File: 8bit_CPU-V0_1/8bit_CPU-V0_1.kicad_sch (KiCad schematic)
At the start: 0 parts

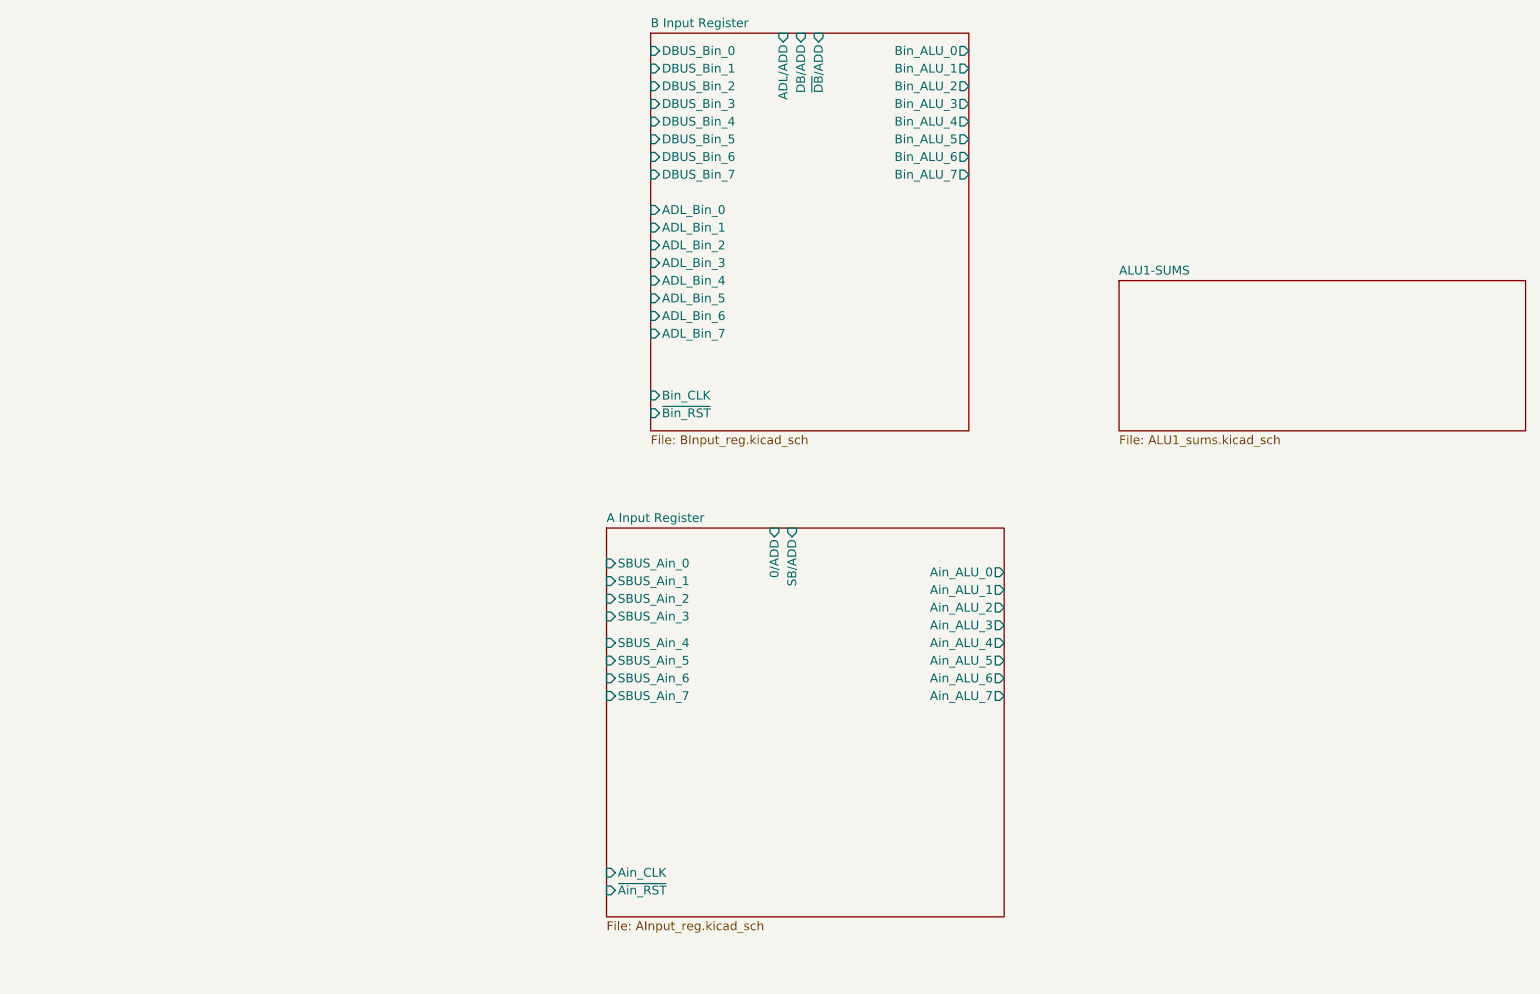
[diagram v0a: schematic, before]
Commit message: Modifications
-Nammed sub parts of circuits
-Created new prepared sheets for ALU ANDS and EORS
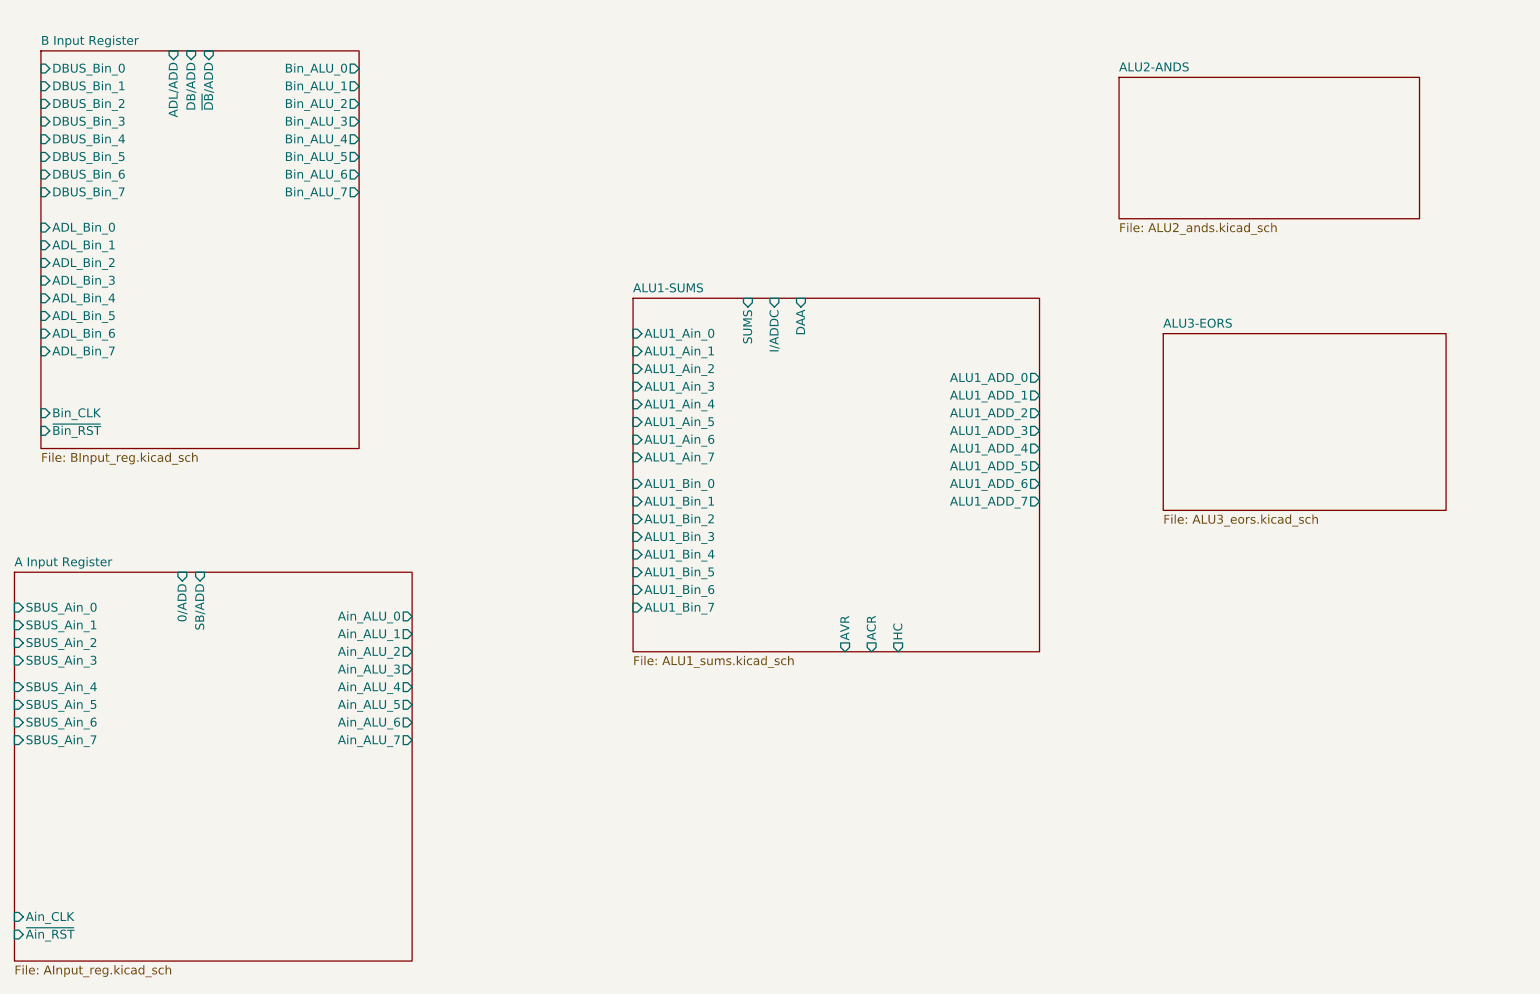
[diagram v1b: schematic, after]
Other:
- added sheet ALU2-ANDS (ALU2_ands.kicad_sch)
- added sheet ALU3-EORS (ALU3_eors.kicad_sch)
- sheet ALU1-SUMS ports: added ACR, ALU1_ADD_0, ALU1_ADD_1, ALU1_ADD_2, ALU1_ADD_3, ALU1_ADD_4, ALU1_ADD_5, ALU1_ADD_6, ALU1_ADD_7, ALU1_Ain_0, ALU1_Ain_1, ALU1_Ain_2, ALU1_Ain_3, ALU1_Ain_4, ALU1_Ain_5, ALU1_Ain_6, ALU1_Ain_7, ALU1_Bin_0, ALU1_Bin_1, ALU1_Bin_2, ALU1_Bin_3, ALU1_Bin_4, ALU1_Bin_5, ALU1_Bin_6, ALU1_Bin_7, AVR, DAA, HC, I/ADDC, SUMS; removed none

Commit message: ALU finished
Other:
- added sheet ALU4-ORS (ALU4_ors.kicad_sch)
- added sheet ALU5-SRS (ALU5_srs.kicad_sch)
- added sheet Adder Hold Register (ADC_register.kicad_sch)
- sheet ALU1-SUMS ports: added SUMS_CARRY(ALU5); removed ACR
- company: (none) -> PRP-DIY
- title: (none) -> PRP-6502 -- Main Schematic

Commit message: ALU finished
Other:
- removed sheet Adder Hold Register
- added sheet Adder Hold Register (ADD) (ADD_register.kicad_sch)
- sheet ALU2-ANDS ports: added ALU2_ADD_0, ALU2_ADD_1, ALU2_ADD_2, ALU2_ADD_3, ALU2_ADD_4, ALU2_ADD_5, ALU2_ADD_6, ALU2_ADD_7, ALU2_Ain_0, ALU2_Ain_1, ALU2_Ain_2, ALU2_Ain_3, ALU2_Ain_4, ALU2_Ain_5, ALU2_Ain_6, ALU2_Ain_7, ALU2_Bin_0, ALU2_Bin_1, ALU2_Bin_2, ALU2_Bin_3, ALU2_Bin_4, ALU2_Bin_5, ALU2_Bin_6, ALU2_Bin_7, ANDS; removed none
- sheet ALU3-EORS ports: added ALU3_ADD_0, ALU3_ADD_1, ALU3_ADD_2, ALU3_ADD_3, ALU3_ADD_4, ALU3_ADD_5, ALU3_ADD_6, ALU3_ADD_7, ALU3_Ain_0, ALU3_Ain_1, ALU3_Ain_2, ALU3_Ain_3, ALU3_Ain_4, ALU3_Ain_5, ALU3_Ain_6, ALU3_Ain_7, ALU3_Bin_0, ALU3_Bin_1, ALU3_Bin_2, ALU3_Bin_3, ALU3_Bin_4, ALU3_Bin_5, ALU3_Bin_6, ALU3_Bin_7, EORS; removed none

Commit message: Refining schematics
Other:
- sheet ALU4-ORS ports: added ALU4_ADD_0, ALU4_ADD_1, ALU4_ADD_2, ALU4_ADD_3, ALU4_ADD_4, ALU4_ADD_5, ALU4_ADD_6, ALU4_ADD_7, ALU4_Ain_0, ALU4_Ain_1, ALU4_Ain_2, ALU4_Ain_3, ALU4_Ain_4, ALU4_Ain_5, ALU4_Ain_6, ALU4_Ain_7, ALU4_Bin_0, ALU4_Bin_1, ALU4_Bin_2, ALU4_Bin_3, ALU4_Bin_4, ALU4_Bin_5, ALU4_Bin_6, ALU4_Bin_7, ORS; removed none
- sheet ALU5-SRS ports: added ACR, ALU5_ADD_0, ALU5_ADD_1, ALU5_ADD_2, ALU5_ADD_3, ALU5_ADD_4, ALU5_ADD_5, ALU5_ADD_6, ALU5_ADD_7, ALU5_Ain_0, ALU5_Ain_1, ALU5_Ain_2, ALU5_Ain_3, ALU5_Ain_4, ALU5_Ain_5, ALU5_Ain_6, ALU5_Ain_7, I/ADDC, SRS, SUMS_CARRY(ALU1); removed none
- sheet Adder Hold Register (ADD) ports: added ADD_ADL_0, ADD_ADL_1, ADD_ADL_2, ADD_ADL_3, ADD_ADL_4, ADD_ADL_5, ADD_ADL_6, ADD_ADL_7, ADD_ALU_0, ADD_ALU_1, ADD_ALU_2, ADD_ALU_3, ADD_ALU_4, ADD_ALU_5, ADD_ALU_6, ADD_ALU_7, ADD_CLK, ADD_SB_0, ADD_SB_1, ADD_SB_2, ADD_SB_3, ADD_SB_4, ADD_SB_5, ADD_SB_6, ADD_SB_7, ADD/ADL, ADD/SB(0-6), ADD/SB(7); removed none
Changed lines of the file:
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@@
     )
   )
-  (sheet (at 114.3 473.71) (size 44.45 31.75) (fields_autoplaced)
+  (sheet (at 118.11 473.71) (size 55.88 33.02) (fields_autoplaced)
     (stroke (width 0.1524) (type solid))
     (fill (color 0 0 0 0.0000))
-    (property "Sheetname" "ALU5-SRS" (at 114.3 472.9984 0)
+    (property "Sheetname" "ALU5-SRS" (at 118.11 472.9984 0)
       (effects (font (size 1.27 1.27)) (justify left bottom))
     )
-    (property "Sheetfile" "ALU5_srs.kicad_sch" (at 114.3 506.0446 0)
+    (property "Sheetfile" "ALU5_srs.kicad_sch" (at 118.11 507.3146 0)
       (effects (font (size 1.27 1.27)) (justify left top))
+    )
+    (pin "ALU5_Ain_3" input (at 118.11 491.49 180)
+      (effects (font (size 1.27 1.27)) (justify left))
+    )
+    (pin "ALU5_Ain_2" input (at 118.11 488.95 180)
+      (effects (font (size 1.27 1.27)) (justify left))
+    )
+    (pin "ALU5_Ain_1" input (at 118.11 486.41 180)
+      (effects (font (size 1.27 1.27)) (justify left))
+    )
+    (pin "ALU5_Ain_4" input (at 118.11 494.03 180)
+      (effects (font (size 1.27 1.27)) (justify left))
+    )
+    (pin "ALU5_Ain_6" input (at 118.11 499.11 180)
+      (effects (font (size 1.27 1.27)) (justify left))
+    )
+    (pin "ALU5_Ain_7" input (at 118.11 501.65 180)
+      (effects (font (size 1.27 1.27)) (justify left))
+    )
+    (pin "ALU5_Ain_5" input (at 118.11 496.57 180)
+      (effects (font (size 1.27 1.27)) (justify left))
+    )
+    (pin "I{slash}ADDC" input (at 138.43 473.71 90)
+      (effects (font (size 1.27 1.27)) (justify right))
+    )
+    (pin "SRS" input (at 142.24 473.71 90)
+      (effects (font (size 1.27 1.27)) (justify right))
+    )
+    (pin "SUMS_CARRY(ALU1)" input (at 146.05 473.71 90)
+      (effects (font (size 1.27 1.27)) (justify right))
+    )
+    (pin "ALU5_Ain_0" input (at 118.11 483.87 180)
+      (effects (font (size 1.27 1.27)) (justify left))
+    )
+    (pin "ACR" output (at 146.05 506.73 270)
+      (effects (font (size 1.27 1.27)) (justify left))
+    )
+    (pin "ALU5_ADD_1" output (at 173.99 483.87 0)
+      (effects (font (size 1.27 1.27)) (justify right))
+    )
+    (pin "ALU5_ADD_2" output (at 173.99 486.41 0)
+      (effects (font (size 1.27 1.27)) (justify right))
+    )
+    (pin "ALU5_ADD_7" output (at 173.99 499.11 0)
+      (effects (font (size 1.27 1.27)) (justify right))
+    )
+    (pin "ALU5_ADD_3" output (at 173.99 488.95 0)
+      (effects (font (size 1.27 1.27)) (justify right))
+    )
+    (pin "ALU5_ADD_4" output (at 173.99 491.49 0)
+      (effects (font (size 1.27 1.27)) (justify right))
+    )
+    (pin "ALU5_ADD_6" output (at 173.99 496.57 0)
+      (effects (font (size 1.27 1.27)) (justify right))
+    )
+    (pin "ALU5_ADD_5" output (at 173.99 494.03 0)
+      (effects (font (size 1.27 1.27)) (justify right))
+    )
+    (pin "ALU5_ADD_0" output (at 173.99 481.33 0)
+      (effects (font (size 1.27 1.27)) (justify right))
     )
     (instances
@@
     )
   )
-  (sheet (at 190.5 300.99) (size 44.45 31.75) (fields_autoplaced)
+  (sheet (at 190.5 300.99) (size 46.99 52.07) (fields_autoplaced)
     (stroke (width 0.1524) (type solid))
     (fill (color 0 0 0 0.0000))
@@
       (effects (font (size 1.27 1.27)) (justify left bottom))
     )
-    (property "Sheetfile" "ADD_register.kicad_sch" (at 190.5 333.3246 0)
+    (property "Sheetfile" "ADD_register.kicad_sch" (at 190.5 353.6446 0)
       (effects (font (size 1.27 1.27)) (justify left top))
+    )
+    (pin "ADD{slash}ADL" input (at 218.44 300.99 90)
+      (effects (font (size 1.27 1.27)) (justify right))
+    )
+    (pin "ADD_ADL_7" output (at 237.49 326.39 0)
+      (effects (font (size 1.27 1.27)) (justify right))
+    )
+    (pin "ADD_ADL_6" output (at 237.49 323.85 0)
+      (effects (font (size 1.27 1.27)) (justify right))
+    )
+    (pin "ADD_ADL_2" output (at 237.49 313.69 0)
+      (effects (font (size 1.27 1.27)) (justify right))
+    )
+    (pin "ADD_ADL_5" output (at 237.49 321.31 0)
+      (effects (font (size 1.27 1.27)) (justify right))
+    )
+    (pin "ADD_ADL_1" output (at 237.49 311.15 0)
+      (effects (font (size 1.27 1.27)) (justify right))
+    )
+    (pin "ADD_ADL_4" output (at 237.49 318.77 0)
+      (effects (font (size 1.27 1.27)) (justify right))
+    )
+    (pin "ADD_ADL_0" output (at 237.49 308.61 0)
+      (effects (font (size 1.27 1.27)) (justify right))
+    )
+    (pin "ADD_ADL_3" output (at 237.49 316.23 0)
+      (effects (font (size 1.27 1.27)) (justify right))
+    )
+    (pin "ADD_SB_1" output (at 237.49 334.01 0)
+      (effects (font (size 1.27 1.27)) (justify right))
+    )
+    (pin "ADD_SB_0" output (at 237.49 331.47 0)
+      (effects (font (size 1.27 1.27)) (justify right))
+    )
+    (pin "ADD_SB_2" output (at 237.49 336.55 0)
+      (effects (font (size 1.27 1.27)) (justify right))
+    )
+    (pin "ADD_SB_5" output (at 237.49 344.17 0)
+      (effects (font (size 1.27 1.27)) (justify right))
+    )
+    (pin "ADD_SB_6" output (at 237.49 346.71 0)
+      (effects (font (size 1.27 1.27)) (justify right))
+    )
+    (pin "ADD_SB_3" output (at 237.49 339.09 0)
+      (effects (font (size 1.27 1.27)) (justify right))
+    )
+    (pin "ADD_SB_4" output (at 237.49 341.63 0)
+      (effects (font (size 1.27 1.27)) (justify right))
+    )
+    (pin "ADD_SB_7" output (at 237.49 349.25 0)
+      (effects (font (size 1.27 1.27)) (justify right))
+    )
+    (pin "ADD{slash}SB(0-6)" input (at 208.28 300.99 90)
+      (effects (font (size 1.27 1.27)) (justify right))
+    )
+    (pin "ADD{slash}SB(7)" input (at 213.36 300.99 90)
+      (effects (font (size 1.27 1.27)) (justify right))
+    )
+    (pin "ADD_ALU_0" input (at 190.5 309.88 180)
+      (effects (font (size 1.27 1.27)) (justify left))
+    )
+    (pin "ADD_ALU_1" input (at 190.5 312.42 180)
+      (effects (font (size 1.27 1.27)) (justify left))
+    )
+    (pin "ADD_ALU_3" input (at 190.5 317.5 180)
+      (effects (font (size 1.27 1.27)) (justify left))
+    )
+    (pin "ADD_ALU_5" input (at 190.5 322.58 180)
+      (effects (font (size 1.27 1.27)) (justify left))
+    )
+    (pin "ADD_ALU_7" input (at 190.5 327.66 180)
+      (effects (font (size 1.27 1.27)) (justify left))
+    )
+    (pin "ADD_ALU_4" input (at 190.5 320.04 180)
+      (effects (font (size 1.27 1.27)) (justify left))
+    )
+    (pin "ADD_ALU_2" input (at 190.5 314.96 180)
+      (effects (font (size 1.27 1.27)) (justify left))
+    )
+    (pin "ADD_CLK" input (at 190.5 341.63 180)
+      (effects (font (size 1.27 1.27)) (justify left))
+    )
+    (pin "ADD_ALU_6" input (at 190.5 325.12 180)
+      (effects (font (size 1.27 1.27)) (justify left))
     )
     (instances
@@
       (effects (font (size 1.27 1.27)) (justify left top))
     )
+    (pin "ORS" input (at 137.16 417.83 90)
+      (effects (font (size 1.27 1.27)) (justify right))
+    )
+    (pin "ALU4_Bin_5" input (at 118.11 455.93 180)
+      (effects (font (size 1.27 1.27)) (justify left))
+    )
+    (pin "ALU4_Bin_3" input (at 118.11 450.85 180)
+      (effects (font (size 1.27 1.27)) (justify left))
+    )
+    (pin "ALU4_Bin_2" input (at 118.11 448.31 180)
+      (effects (font (size 1.27 1.27)) (justify left))
+    )
+    (pin "ALU4_Bin_7" input (at 118.11 461.01 180)
+      (effects (font (size 1.27 1.27)) (justify left))
+    )
+    (pin "ALU4_Bin_4" input (at 118.11 453.39 180)
+      (effects (font (size 1.27 1.27)) (justify left))
+    )
+    (pin "ALU4_Bin_6" input (at 118.11 458.47 180)
+      (effects (font (size 1.27 1.27)) (justify left))
+    )
+    (pin "ALU4_Bin_1" input (at 118.11 445.77 180)
+      (effects (font (size 1.27 1.27)) (justify left))
+    )
+    (pin "ALU4_Bin_0" input (at 118.11 443.23 180)
+      (effects (font (size 1.27 1.27)) (justify left))
+    )
+    (pin "ALU4_Ain_7" input (at 118.11 438.15 180)
+      (effects (font (size 1.27 1.27)) (justify left))
+    )
+    (pin "ALU4_Ain_6" input (at 118.11 435.61 180)
+      (effects (font (size 1.27 1.27)) (justify left))
+    )
+    (pin "ALU4_Ain_5" input (at 118.11 433.07 180)
+      (effects (font (size 1.27 1.27)) (justify left))
+    )
+    (pin "ALU4_ADD_6" output (at 173.99 443.23 0)
+      (effects (font (size 1.27 1.27)) (justify right))
+    )
+    (pin "ALU4_ADD_5" output (at 173.99 440.69 0)
+      (effects (font (size 1.27 1.27)) (justify right))
+    )
+    (pin "ALU4_ADD_7" output (at 173.99 445.77 0)
+      (effects (font (size 1.27 1.27)) (justify right))
+    )
+    (pin "ALU4_ADD_0" output (at 173.99 427.99 0)
+      (effects (font (size 1.27 1.27)) (justify right))
+    )
+    (pin "ALU4_ADD_2" output (at 173.99 433.07 0)
+      (effects (font (size 1.27 1.27)) (justify right))
+    )
+    (pin "ALU4_ADD_1" output (at 173.99 430.53 0)
+      (effects (font (size 1.27 1.27)) (justify right))
+    )
+    (pin "ALU4_ADD_4" output (at 173.99 438.15 0)
+      (effects (font (size 1.27 1.27)) (justify right))
+    )
+    (pin "ALU4_ADD_3" output (at 173.99 435.61 0)
+      (effects (font (size 1.27 1.27)) (justify right))
+    )
+    (pin "ALU4_Ain_1" input (at 118.11 422.91 180)
+      (effects (font (size 1.27 1.27)) (justify left))
+    )
+    (pin "ALU4_Ain_0" input (at 118.11 420.37 180)
+      (effects (font (size 1.27 1.27)) (justify left))
+    )
+    (pin "ALU4_Ain_2" input (at 118.11 425.45 180)
+      (effects (font (size 1.27 1.27)) (justify left))
+    )
+    (pin "ALU4_Ain_3" input (at 118.11 427.99 180)
+      (effects (font (size 1.27 1.27)) (justify left))
+    )
+    (pin "ALU4_Ain_4" input (at 118.11 430.53 180)
+      (effects (font (size 1.27 1.27)) (justify left))
+    )
     (instances

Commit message: update.
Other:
- added sheet Accumulator (AC) (Accumulator.kicad_sch)
- added sheet Clock Generator (CLK_gen.kicad_sch)
- added sheet Decimal adjuster Adders (Decimal adjustet.kicad_sch)
- added sheet Overflow dectection (OVR_det.kicad_sch)
- added sheet Program Counter Low (PCL & PCLS) (PCL.kicad_sch)
